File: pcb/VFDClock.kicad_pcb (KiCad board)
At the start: 4 copper layers, 80 x 52.7 mm, 84 parts, among them J1 Conn_01x04_Socket, J2 R_SIG_CONN, J3 R_PWR_CONN, J4 USB_C_Receptacle_USB2.0_16P, J5 L_SIG_CONN, J6 L_PWR_CONN, J7 CONN_GPIO, J8 L_COL_CONN, J9 R_COL_CONN, SW1 SW_SPST, SW2 SW_SPST, SW3 SW_SPST, SW4 SW_SPST, SW5 SW_SPST, SW6 SW_SPST, U1 TBD62783AFWG, U10 AMS1117-1.5, U2 ESP32-S3-WROOM-1, U3 IP4234CZ6, U4 TBD62783AFNG, U5 SN74HC595PWR, U6 AMS1117-3.3, U7 DS3231MZ+TRL, U8 SHT45-AD1B-R2, U9 VEML3235SL

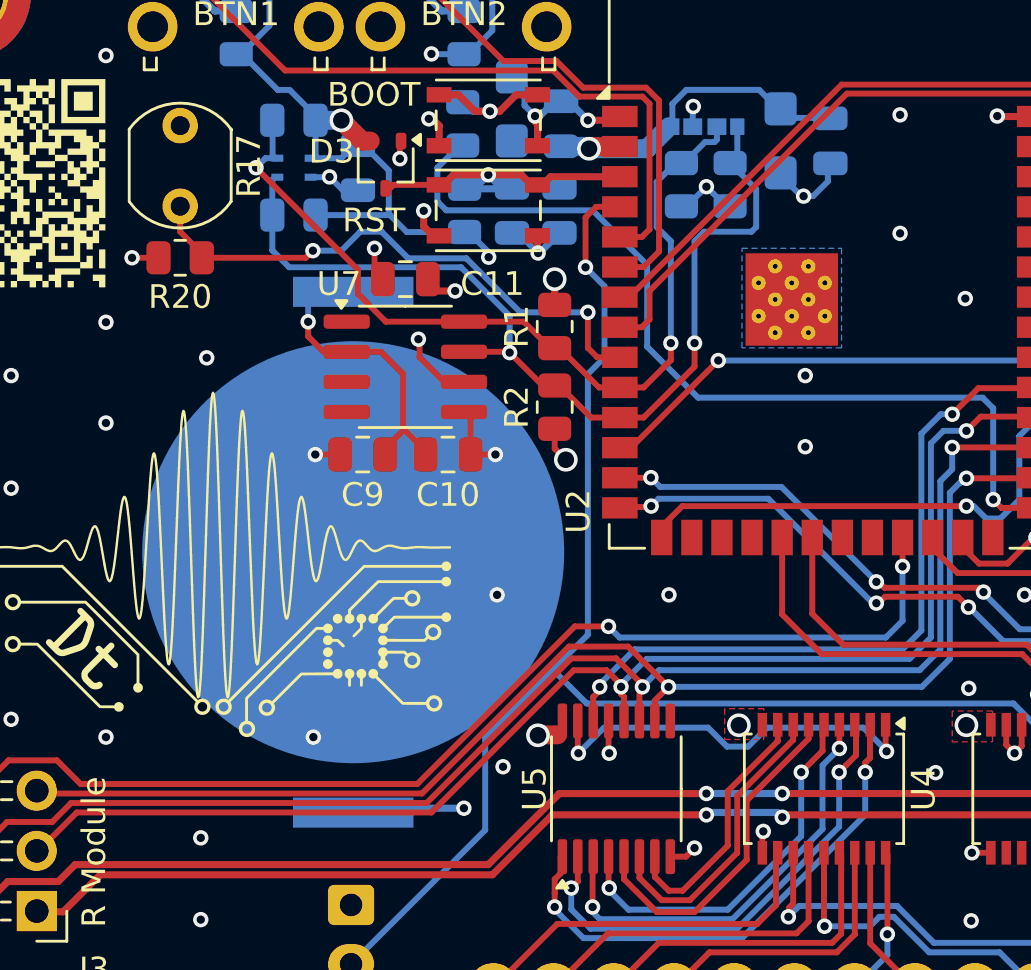
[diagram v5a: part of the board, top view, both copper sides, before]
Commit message: Moved cell battery, generated STEP files
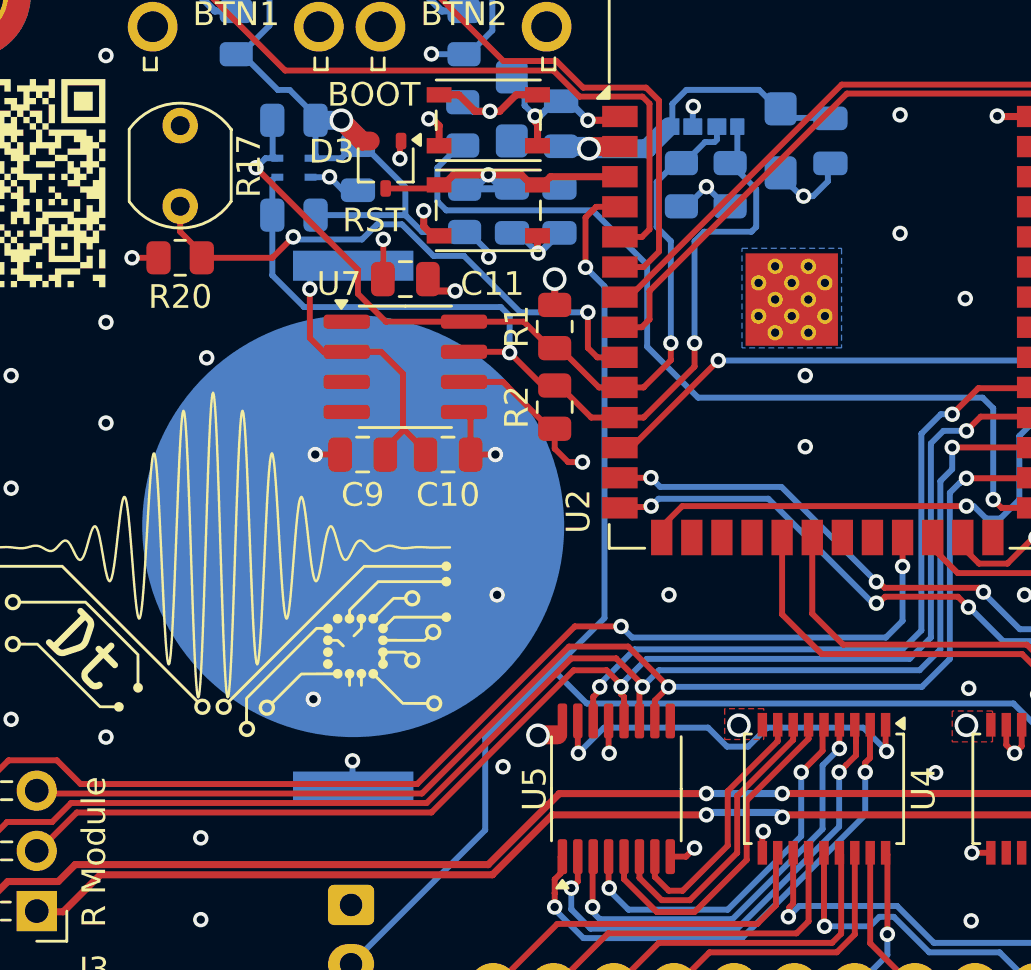
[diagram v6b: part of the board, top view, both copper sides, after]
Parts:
- moved BT1 1.10 mm to (128.9, 105.6)
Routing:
- net Vbat: track 43.0 -> 36.2 mm
- net +3V3: track 263.9 -> 264.6 mm, vias 14 -> 13
- net /SDA: track 40.8 -> 41.4 mm
